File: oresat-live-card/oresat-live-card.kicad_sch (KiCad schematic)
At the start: 7 parts

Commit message: Changed to hierarchy view
updated OPD and component symbols. Resolved all DRC errors and warnings.
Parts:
- added J1: SM14B-SHLS-TF, oresat-connectors:J-JST-SM14BSHLSTF, symbol oresat-connectors:ORESAT-DEBUG-CONNECTOR-3
- added J10, J2: SM06B-SRSS-TB, oresat-live-card:CONN_SM06B-SRSS-TB_JST, symbol oresat-connectors:SM06B-SRSS-TB(LF)(SN)
- added J4: TFM-120-01-L-D-RA, oresat-connectors:J-SAMTEC-TFM-120-X1-XXX-D-RA, symbol oresat-connectors:J-SAMTEC-TFM-120-01-L-D-RA
- added J6, J8: SMPM, oresat-connectors:J-MOLEX-SMPM-073300-002X, symbol oresat-connectors:J-MOLEX-SMPM-73300-002X
- added TP159: 0.03x0.04, oresat-misc:TestPoint-0.75mm-th, symbol oresat-misc:Test-Point-1mm-round
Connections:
- new net: J1.8 (DEBUG-0), TP159.1
- new net C3-UART-RX: J4.38
- new net C3-UART-TX: J4.37
- new net CAN2_H: J4.17, J4.18
- new net CAN2_L: J4.19, J4.20
- new net GND: J1.14 (GND), J1.15 (PAD), J1.16 (PAD), J1.5 (GND), J10.3, J10.7, J10.8 (7), J2.3, J2.7, J2.8 (7), J4.27, J4.28, J4.29, J4.30, J6.SHLD, J8.SHLD
- new net OPD_PWR: J4.15, J4.16
- new net OPD_SCL: J4.13, J4.14
- new net OPD_SDA: J4.11, J4.12
- new net UART0_RX: J1.7 (CARD-RX)
- new net UART0_TX: J1.6 (CARD-TX)
- new net USB HUB/CAMERA_USB_N: J10.4
- new net USB HUB/CAMERA_USB_P: J10.5
- new net USB HUB/CAMERA_VUSB: J10.6
- new net USB HUB/WIFI_ENABLE: J2.1
- new net USB HUB/WIFI_STATUS: J2.2
- new net USB HUB/WIFI_USB_N: J2.5
- new net USB HUB/WIFI_USB_P: J2.4
- new net USB HUB/WIFI_VUSB: J2.6
- new net USB_DEV_N: J1.4 (DEVICE-D-)
- new net USB_DEV_P: J1.3 (DEVICE-D+)
- new net USB_DEV_VBUS: J1.1 (VBUSP), J1.2 (VBUSP)
- new net VBUS: J4.23, J4.24, J4.25, J4.26
- new net WiFi Switching/HELICAL_ANTENNA: J6.SIG
- new net WiFi Switching/PATCH_ANTENNA: J8.SIG
- new net nRESET: J1.10 (NRST)
- no-connect marks 0 -> 26
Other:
- sheet SIP B: USB + ADC + Crystals renamed SIP B: ADC + Crystals
- removed sheet Connectors
- added sheet USB HUB (oresat-live-card-sch-usb-hub.kicad_sch)
- sheet Power + OPD ports: added C3-UART-RX, C3-UART-TX, OPD_PWR, OPD_SCL, OPD_SDA, SYSBOOT2, UART0_RX, UART0_TX; removed none
- sheet SIP A: Power ports: added VIN_USB, nRESET, nRESET_CLAMP; removed none
- sheet SIP B: ADC + Crystals ports: added PA_THERMISTOR, RX_DET_OUT, UP_N, UP_P, USB_DEV_N, USB_DEV_P, USB_DEV_VBUS, USB_VBUS, VIN_USB, nRESET_CLAMP; removed none
- sheet SIP C: SD + eMMC + CAN ports: added CAN2_H, CAN2_L, GRSTz, UART0_RX, UART0_TX; removed none
- sheet SIP D: Boot ports: added ANT_SEL, SYSBOOT2, TRANSMIT; removed none
- sheet WiFi LNA ports: added PA_ON_LNA_OFF, RX_DET_OUT, RX_IN; removed none
- sheet WiFi PA ports: added PA_MATCH_OUT, PA_ON_LNA_OFF, PA_THERMISTOR; removed none
- sheet WiFi Switching ports: added ANT_SEL, HELICAL_ANTENNA, PATCH_ANTENNA, PA_MATCH_OUT, PA_ON_LNA_OFF, RX_IN, TRANSMIT; removed none
- note added: "Cable to camera: Cut JST A06SE06SR30K102A in half and solder directly to Camera board"
- note added: "Cable to wifi: JST A06SR06SR30K51A"
- note added: "Main Connector"
- note added: "Main OreSat Card Connector"
- note added: "Oresat Debug Connector"
- note added: "RF Connectors"
- moved on the sheet: FID1, FID2, FID3, FID4, FID5, FID6

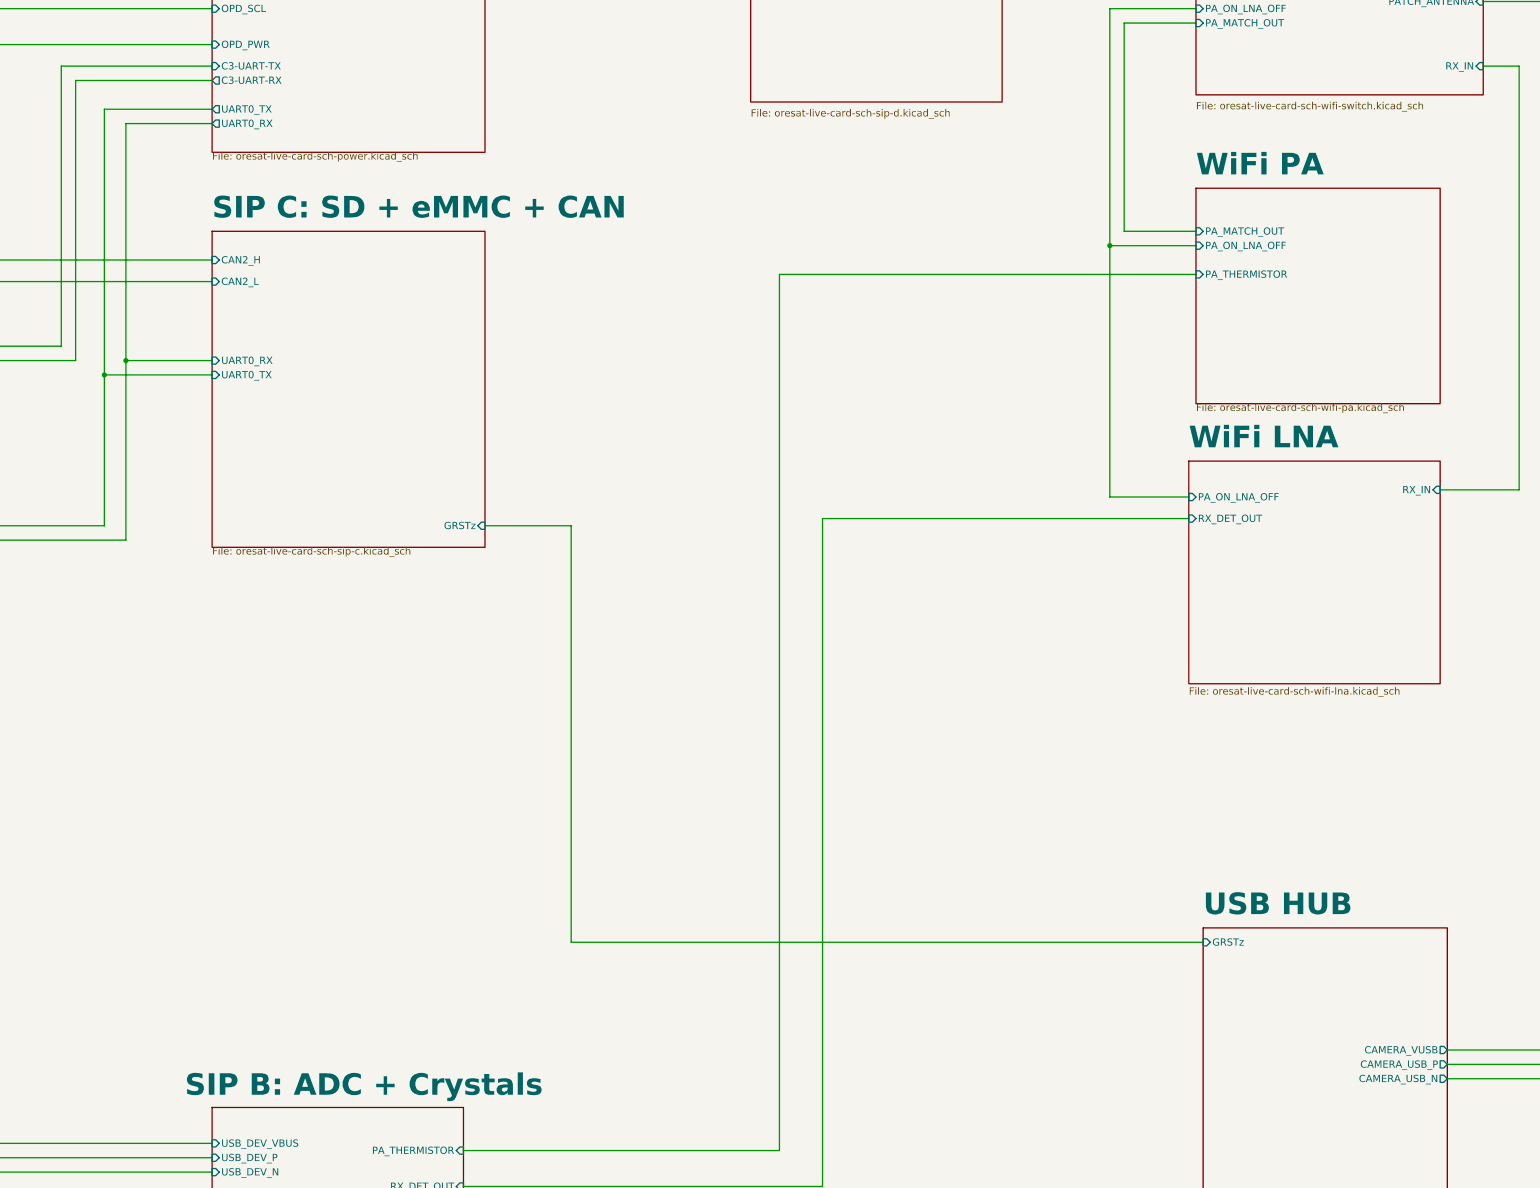
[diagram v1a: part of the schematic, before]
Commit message: Schematic Update
Updated Schematic to help alleviate some of the DRC errors and warnings.
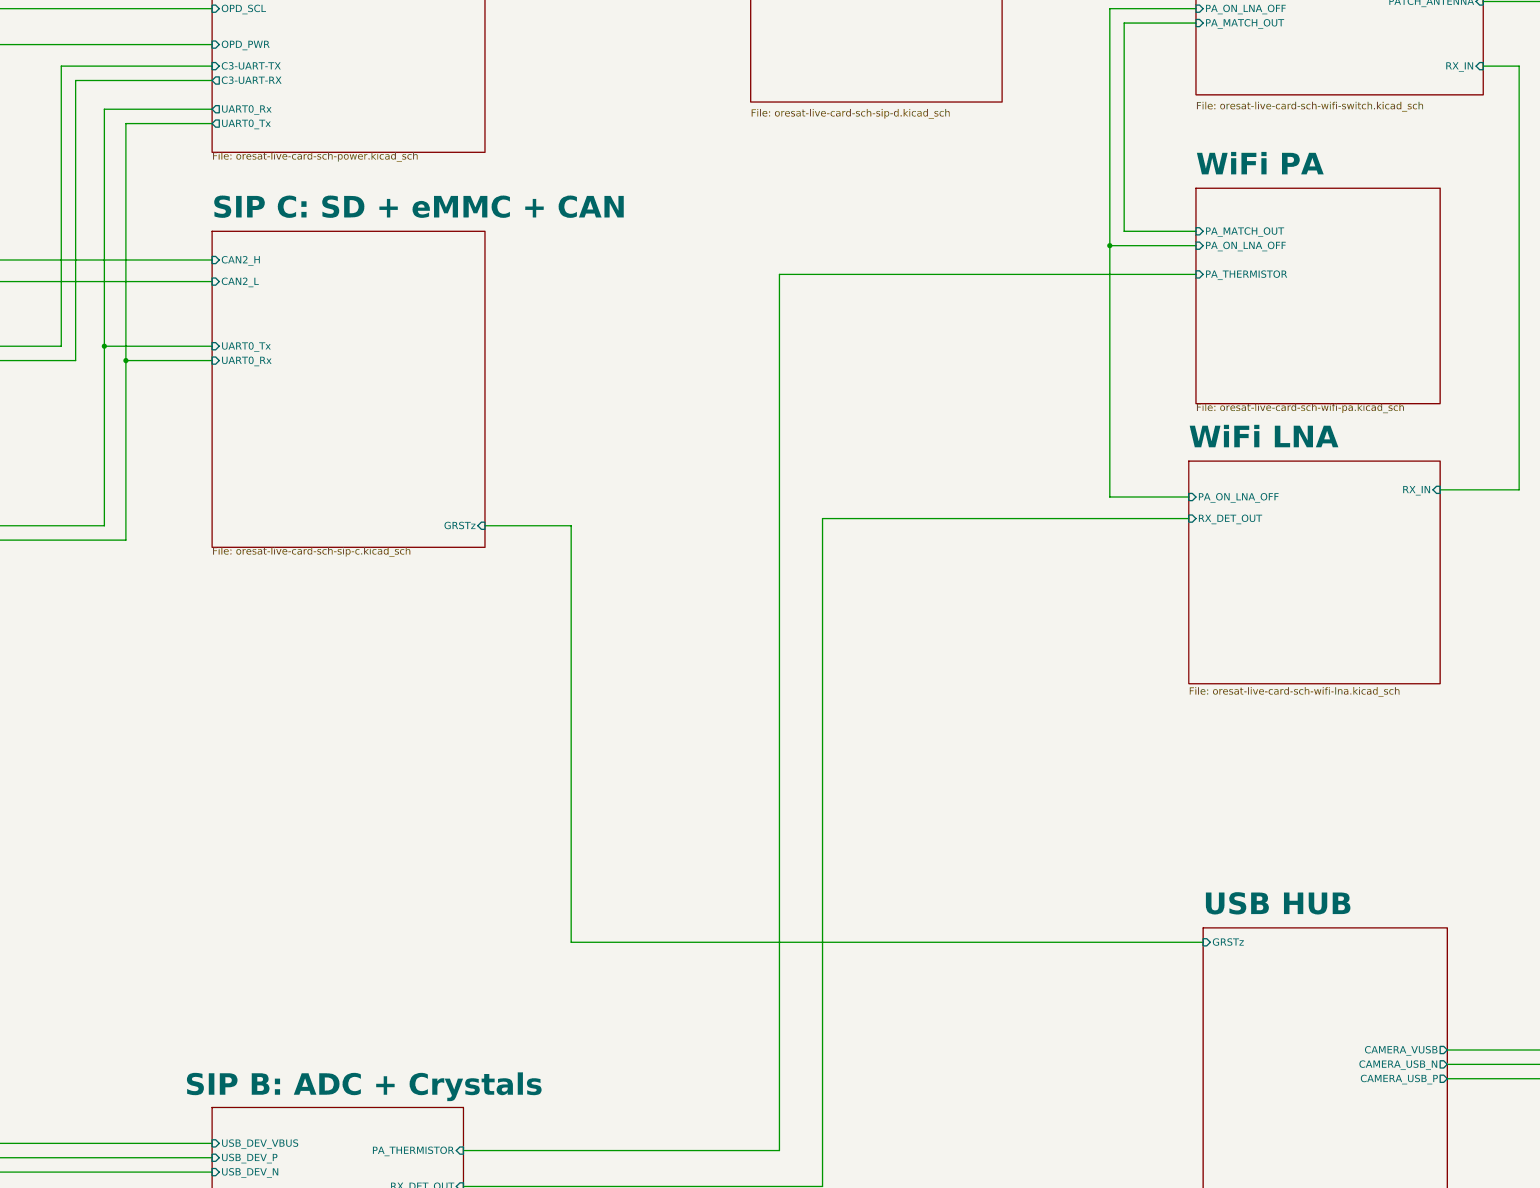
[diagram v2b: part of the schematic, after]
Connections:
- net USB HUB/CAMERA_USB_N: now also J10.5; no longer J10.4
- net USB HUB/CAMERA_USB_P: now also J10.4; no longer J10.5
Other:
- sheet Power + OPD ports: added UART0_Rx, UART0_Tx; removed UART0_RX, UART0_TX
- sheet SIP C: SD + eMMC + CAN ports: added UART0_Rx, UART0_Tx; removed UART0_RX, UART0_TX
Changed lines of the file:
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@@
 	)
 	(junction
-		(at 171.45 143.51)
+		(at 349.25 120.65)
 		(diameter 0)
 		(color 0 0 0 0)
 	)
 	(junction
-		(at 349.25 120.65)
+		(at 171.45 138.43)
 		(diameter 0)
 		(color 0 0 0 0)
@@
 	(wire
 		(pts
+			(xy 408.94 265.43) (xy 502.92 265.43)
+		)
+		(stroke
+			(width 0)
+			(type default)
+		)
+	)
+	(wire
+		(pts
 			(xy 52.07 92.71) (xy 58.42 92.71)
 		)
@@
 	(wire
 		(pts
-			(xy 408.94 265.43) (xy 502.92 265.43)
+			(xy 408.94 267.97) (xy 502.92 267.97)
 		)
 		(stroke
@@
 	(wire
 		(pts
-			(xy 171.45 143.51) (xy 190.5 143.51)
+			(xy 171.45 138.43) (xy 190.5 138.43)
 		)
 		(stroke
@@
 	(wire
 		(pts
-			(xy 408.94 267.97) (xy 502.92 267.97)
-		)
-		(stroke
-			(width 0)
-			(type default)
-		)
-	)
-	(wire
-		(pts
 			(xy 58.42 78.74) (xy 190.5 78.74)
 		)
@@
 	(wire
 		(pts
-			(xy 171.45 96.52) (xy 171.45 143.51)
+			(xy 171.45 96.52) (xy 171.45 138.43)
 		)
 		(stroke
@@
 	(wire
 		(pts
-			(xy 171.45 143.51) (xy 171.45 170.18)
+			(xy 171.45 138.43) (xy 171.45 170.18)
 		)
 		(stroke
@@
 			)
 		)
-		(pin "UART0_RX" input
-			(at 190.5 140.97 180)
+		(pin "GRSTz" input
+			(at 238.76 170.18 0)
 			(effects
 				(font
 					(size 1.27 1.27)
 				)
-				(justify left)
+				(justify right)
 			)
 		)
-		(pin "UART0_TX" input
-			(at 190.5 143.51 180)
+		(pin "UART0_Rx" input
+			(at 190.5 140.97 180)
 			(effects
 				(font
@@
 			)
 		)
-		(pin "GRSTz" input
-			(at 238.76 170.18 0)
+		(pin "UART0_Tx" input
+			(at 190.5 138.43 180)
 			(effects
 				(font
 					(size 1.27 1.27)
 				)
-				(justify right)
+				(justify left)
 			)
 		)
@@
 			)
 		)
-		(pin "UART0_RX" output
-			(at 190.5 99.06 180)
+		(pin "OPD_PWR" input
+			(at 190.5 85.09 180)
 			(effects
 				(font
@@
 			)
 		)
-		(pin "UART0_TX" output
+		(pin "UART0_Rx" output
 			(at 190.5 96.52 180)
 			(effects
@@
 			)
 		)
-		(pin "OPD_PWR" input
-			(at 190.5 85.09 180)
+		(pin "UART0_Tx" output
+			(at 190.5 99.06 180)
 			(effects
 				(font
@@
 		)
 		(pin "CAMERA_USB_P" output
-			(at 408.94 265.43 0)
+			(at 408.94 267.97 0)
 			(effects
 				(font
@@
 		)
 		(pin "CAMERA_USB_N" output
-			(at 408.94 267.97 0)
+			(at 408.94 265.43 0)
 			(effects
 				(font

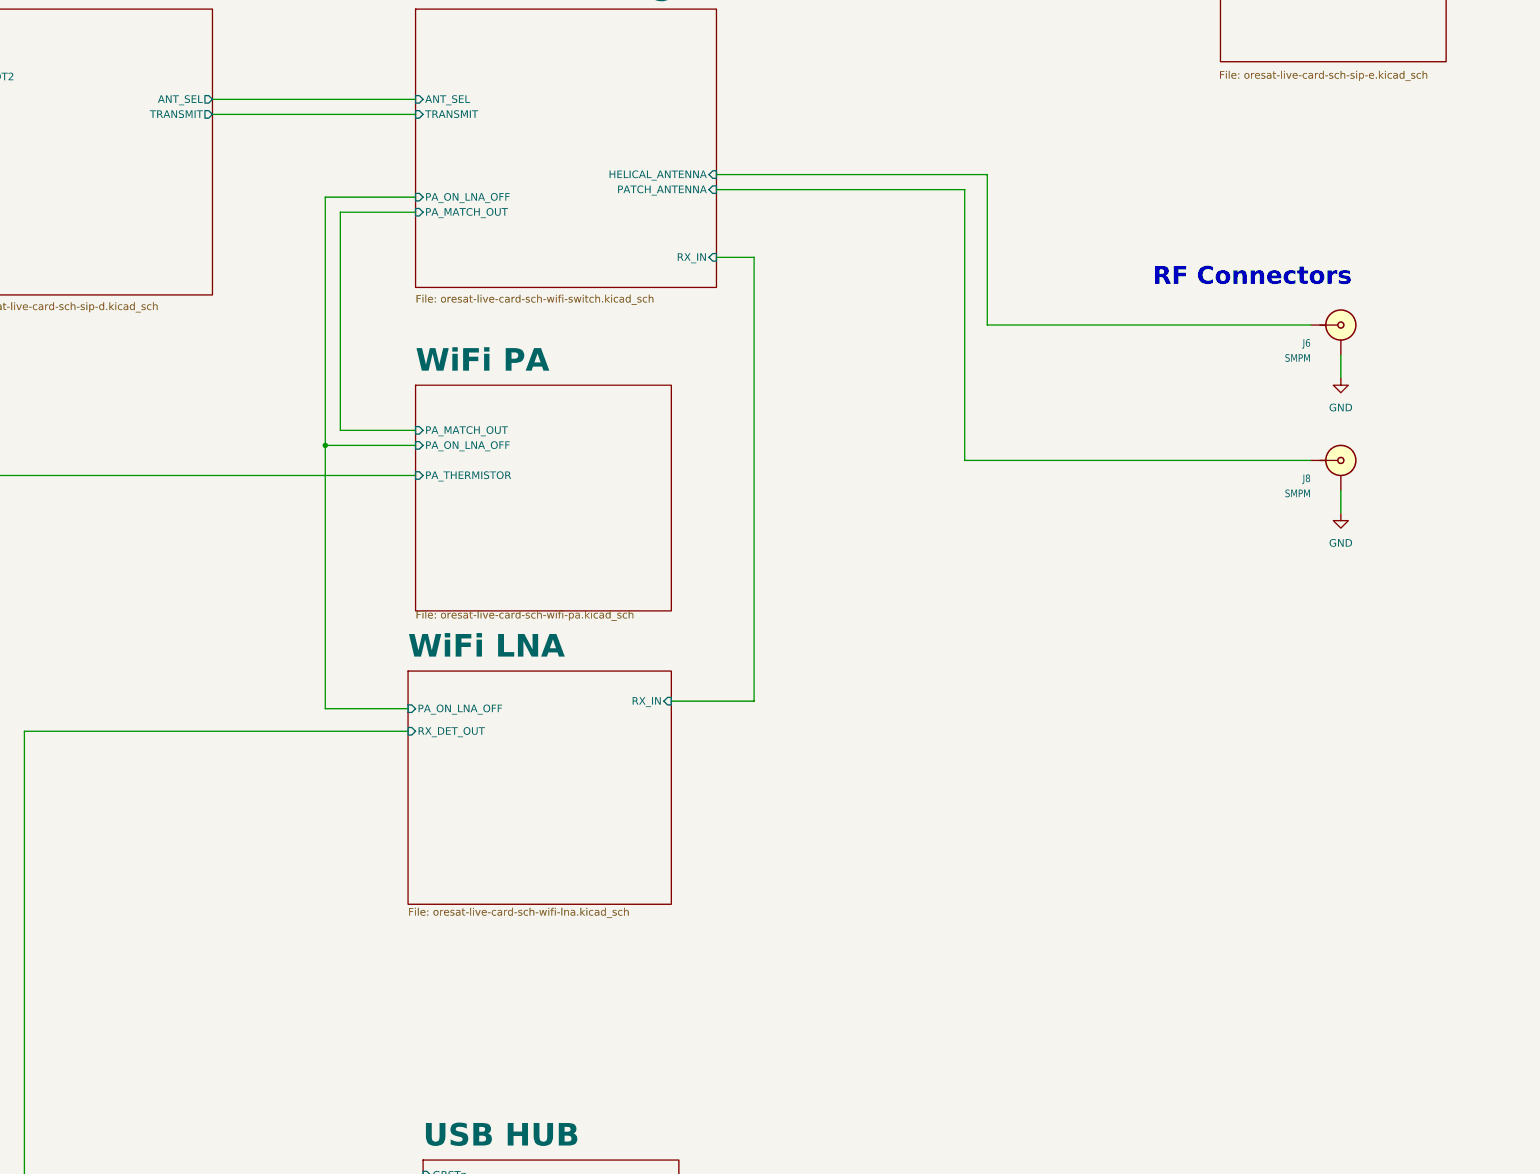
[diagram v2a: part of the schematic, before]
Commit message: Organizational changes
Updated hierarchical labels and other misc schematic fixes
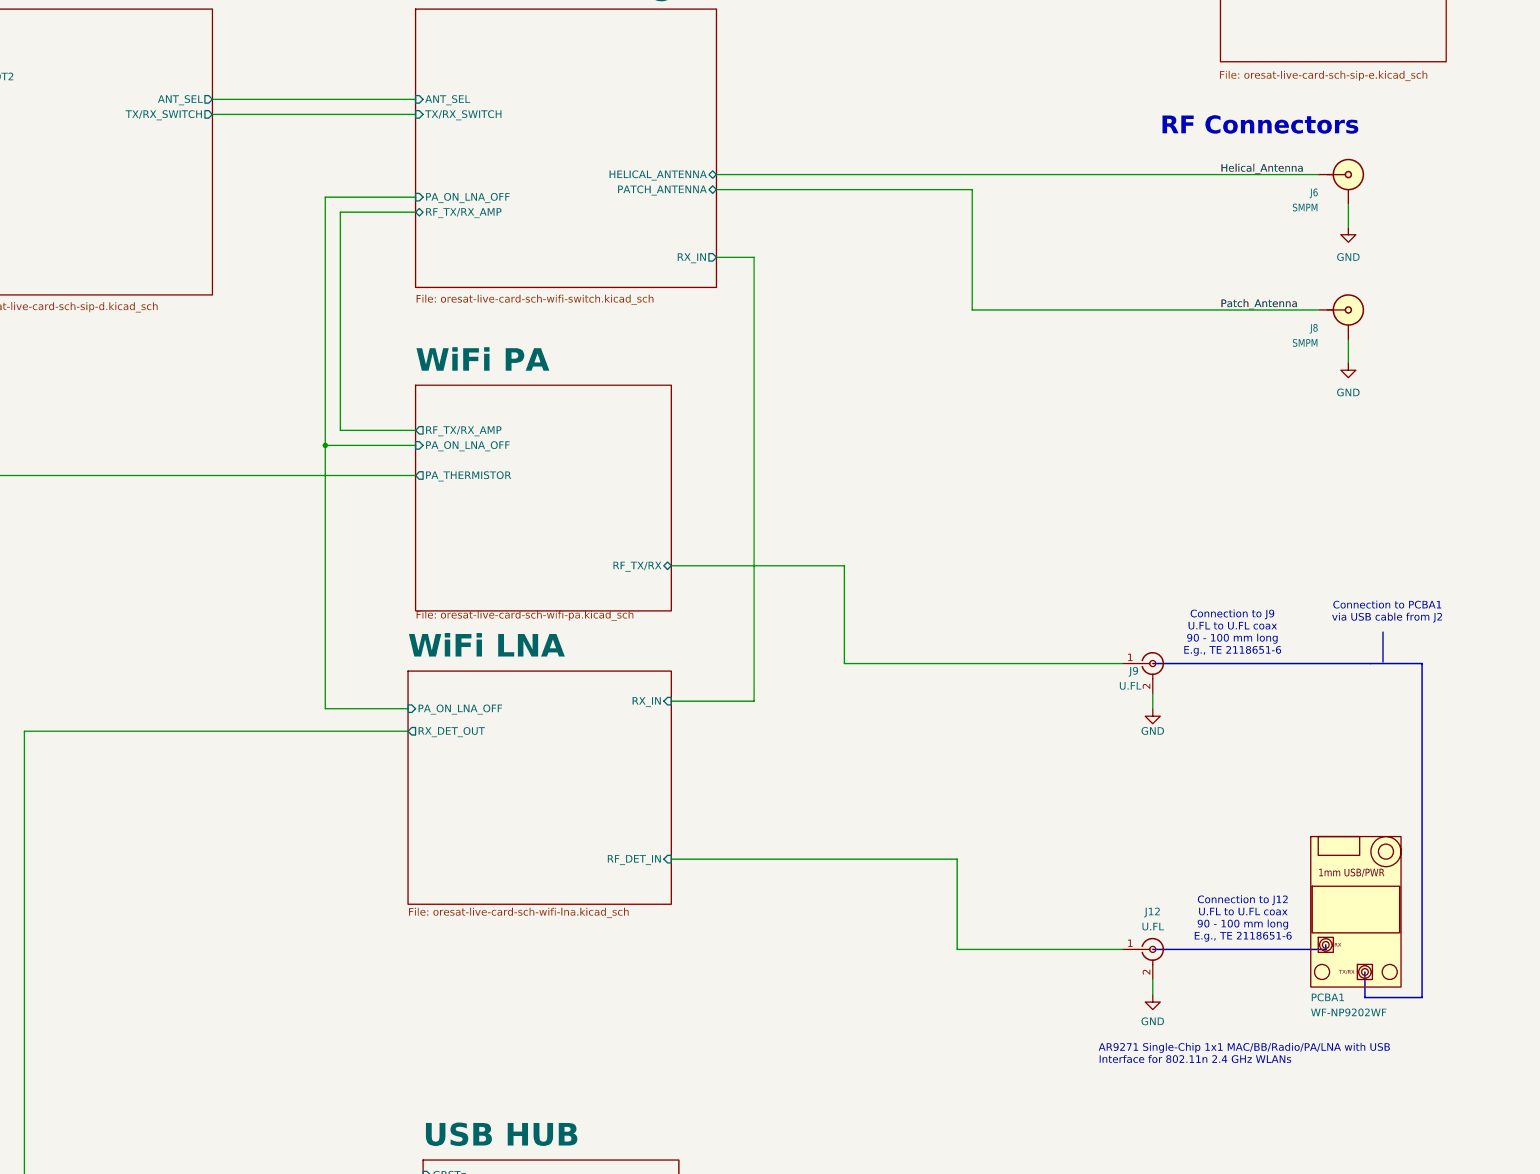
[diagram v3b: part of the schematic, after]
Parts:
- added J12, J9: U.FL, Connector_Coaxial:U.FL_Molex_MCRF_73412-0110_Vertical, symbol Connector:Conn_Coaxial
- added PCBA1: WF-NP9202WF, oresat-live-card:WF-NP9202, symbol oresat-pcbs:WF-NP9202WF
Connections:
- net GND: now also J6.2 (SHLD), J8.2 (SHLD), J12.2 (Ext), J9.2 (Ext); no longer J6.SHLD, J8.SHLD
- removed net WiFi Switching/HELICAL_ANTENNA: J6.SIG
- removed net WiFi Switching/PATCH_ANTENNA: J8.SIG
- new net Helical_Antenna: J6.1 (SIG)
- new net Patch_Antenna: J8.1 (SIG)
- new net WiFi LNA/RF_DET_IN: J12.1 (In)
- new net WiFi PA/RF_TX/RX: J9.1 (In)
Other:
- sheet SIP D: Boot ports: added TX/RX_SWITCH; removed TRANSMIT
- sheet WiFi LNA ports: added RF_DET_IN; removed none
- sheet WiFi PA ports: added RF_TX/RX, RF_TX/RX_AMP; removed PA_MATCH_OUT
- sheet WiFi Switching ports: added RF_TX/RX_AMP, TX/RX_SWITCH; removed PA_MATCH_OUT, TRANSMIT
- note added: "AR9271 Single-Chip 1x1 MAC/BB/Radio/PA/LNA with USB Interface for 802.11n 2.4 GHz WLANs"
- note added: "Connection to J12 U.FL to U.FL coax 90 - 100 mm long E.g., TE 2118651-6"
- note added: "Connection to J9 U.FL to U.FL coax 90 - 100 mm long E.g., TE 2118651-6"
- note added: "Connection to PCBA1 via USB cable from J2"
- moved on the sheet: J6, J8

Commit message: Schematic and PCB update
updated hierarchy labels to have more clarifying names. Fixed RF connector symbol to footprint issues. Linked footprints and 3d models. Added DRC error clearance to ignore of specific RF class. Fixed most of all the DRC warnings and errors outside emmc and silkscreen on exposed copper
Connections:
- net Helical_Antenna renamed HEL_ANT
- net Patch_Antenna renamed PATCH_ANT
- net WiFi PA/RF_TX/RX renamed WiFi PA/RF_TX
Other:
- sheet Power + OPD ports: added UART0_RX, UART0_TX; removed UART0_Rx, UART0_Tx
- sheet SIP B: ADC + Crystals ports: added RF/RX_IN_DETECTED; removed RX_DET_OUT
- sheet SIP C: SD + eMMC + CAN ports: added UART0_RX, UART0_TX; removed UART0_Rx, UART0_Tx
- sheet WiFi LNA ports: added LNA_SHUTDOWN, RF/RX_IN_DETECTED; removed PA_ON_LNA_OFF, RX_DET_OUT
- sheet WiFi PA ports: added RF_TX, RF_TX_AMP, TOGGLE_PA; removed PA_ON_LNA_OFF, RF_TX/RX, RF_TX/RX_AMP
- sheet WiFi Switching ports: added RF_TX_AMP; removed RF_TX/RX_AMP
- moved on the sheet: PCBA1
